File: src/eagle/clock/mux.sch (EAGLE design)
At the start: 53 parts, among them U1 SN74HC595N, U2 SN74HC595N, U3 SN74HC595N

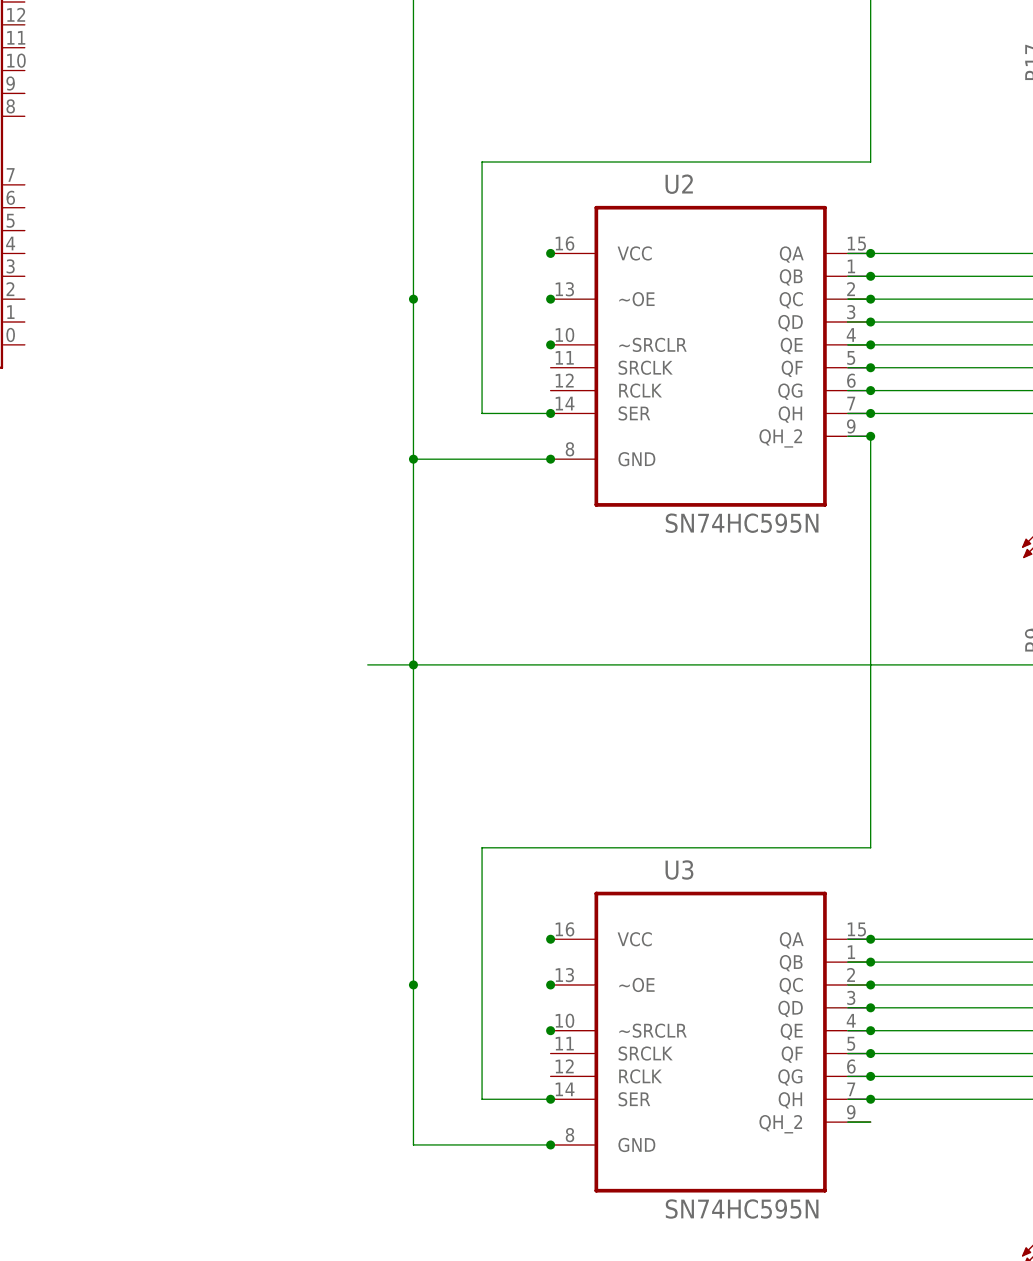
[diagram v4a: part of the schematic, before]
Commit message: cleaner connections between AR11=>SRSER
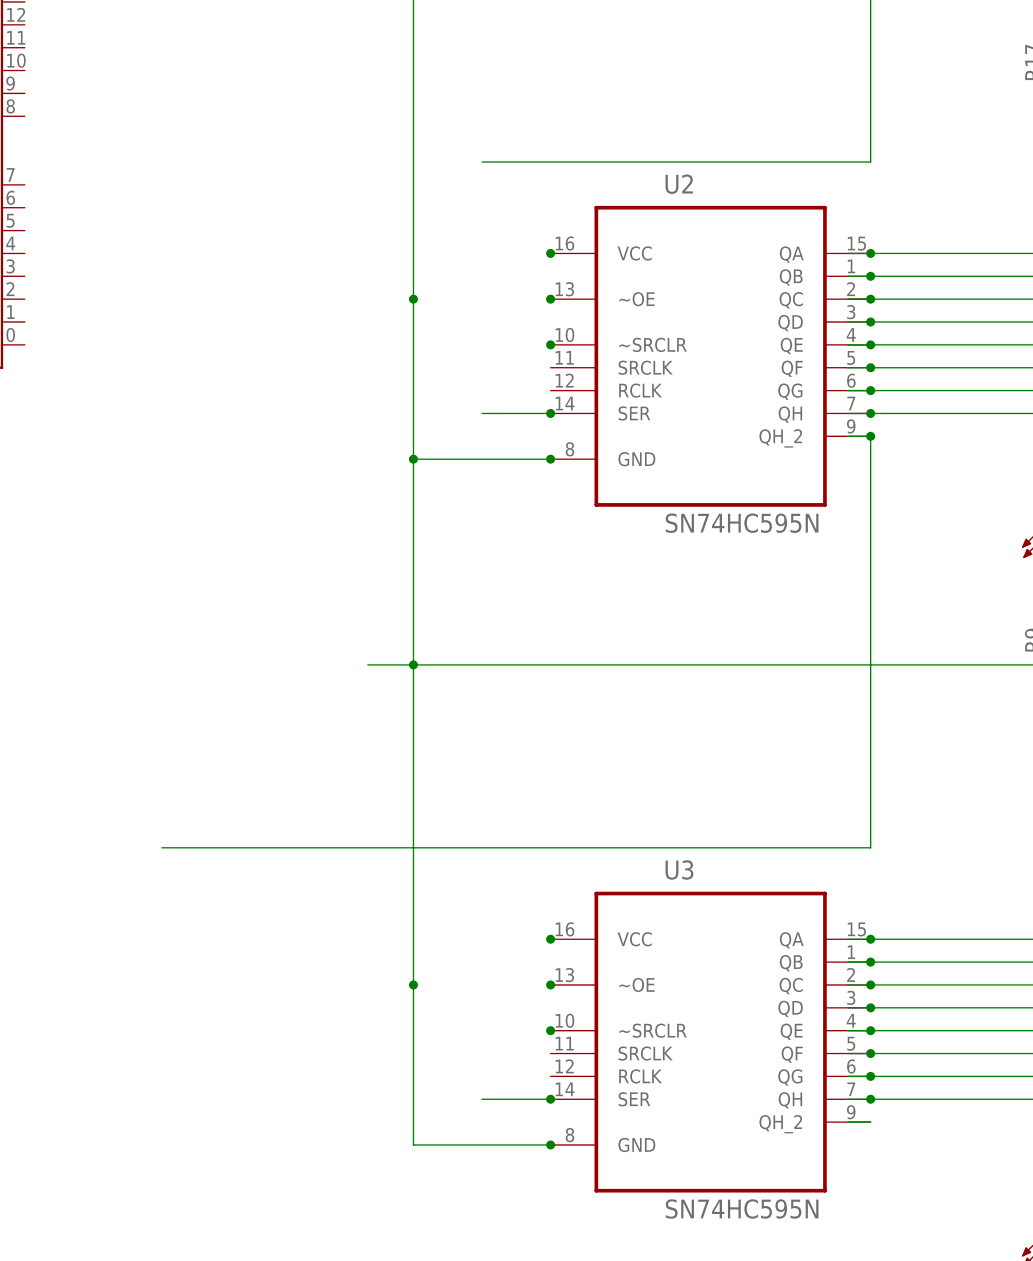
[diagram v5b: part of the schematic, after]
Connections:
- new net N$66: U2.SER
- new net N$67: U3.SER
- net N$25: no longer U2.SER
- net N$28: no longer U3.SER
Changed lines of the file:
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@@
 <wire x1="-7.62" y1="60.96" x2="-7.62" y2="50.8" width="0.1524" layer="93"/>
 <wire x1="-7.62" y1="50.8" x2="-7.62" y2="-2.54" width="0.1524" layer="93"/>
-<wire x1="-7.62" y1="-2.54" x2="20.32" y2="-2.54" width="0.1524" layer="93"/>
+<wire x1="-7.62" y1="-2.54" x2="2.54" y2="-2.54" width="0.1524" layer="93"/>
+<wire x1="7.62" y1="-2.54" x2="20.32" y2="-2.54" width="0.1524" layer="93"/>
 <wire x1="0" y1="-48.26" x2="-116.84" y2="-48.26" width="0.1524" layer="93"/>
 <wire x1="-116.84" y1="-48.26" x2="-116.84" y2="10.16" width="0.1524" layer="93"/>
@@
 <wire x1="-116.84" y1="60.96" x2="-7.62" y2="60.96" width="0.1524" layer="93"/>
 <wire x1="20.32" y1="55.88" x2="5.08" y2="55.88" width="0.1524" layer="93"/>
-<wire x1="5.08" y1="55.88" x2="5.08" y2="38.1" width="0.1524" layer="93"/>
+<wire x1="5.08" y1="55.88" x2="5.08" y2="53.34" width="0.1524" layer="93"/>
+<wire x1="5.08" y1="48.26" x2="5.08" y2="45.72" width="0.1524" layer="93"/>
+<wire x1="5.08" y1="40.64" x2="5.08" y2="38.1" width="0.1524" layer="93"/>
 <wire x1="20.32" y1="-7.62" x2="5.08" y2="-7.62" width="0.1524" layer="93"/>
 <wire x1="20.32" y1="-83.82" x2="5.08" y2="-83.82" width="0.1524" layer="93"/>
 <wire x1="20.32" y1="50.8" x2="-7.62" y2="50.8" width="0.1524" layer="93"/>
-<wire x1="20.32" y1="-12.7" x2="-7.62" y2="-12.7" width="0.1524" layer="93"/>
-<wire x1="20.32" y1="-88.9" x2="-7.62" y2="-88.9" width="0.1524" layer="93"/>
-<wire x1="-7.62" y1="-78.74" x2="20.32" y2="-78.74" width="0.1524" layer="93"/>
+<wire x1="20.32" y1="-12.7" x2="7.62" y2="-12.7" width="0.1524" layer="93"/>
+<wire x1="2.54" y1="-12.7" x2="-7.62" y2="-12.7" width="0.1524" layer="93"/>
+<wire x1="20.32" y1="-88.9" x2="7.62" y2="-88.9" width="0.1524" layer="93"/>
+<wire x1="2.54" y1="-88.9" x2="-7.62" y2="-88.9" width="0.1524" layer="93"/>
+<wire x1="-7.62" y1="-78.74" x2="2.54" y2="-78.74" width="0.1524" layer="93"/>
+<wire x1="7.62" y1="-78.74" x2="20.32" y2="-78.74" width="0.1524" layer="93"/>
+<wire x1="-38.1" y1="20.32" x2="-22.86" y2="20.32" width="0.1524" layer="93"/>
+<wire x1="-22.86" y1="20.32" x2="-22.86" y2="43.18" width="0.1524" layer="93"/>
+<wire x1="-22.86" y1="43.18" x2="-10.16" y2="43.18" width="0.1524" layer="93"/>
+<wire x1="-5.08" y1="43.18" x2="20.32" y2="43.18" width="0.1524" layer="93"/>
+<wire x1="-10.16" y1="43.18" x2="-5.08" y2="43.18" width="0.1524" layer="93" curve="-180"/>
+<wire x1="5.08" y1="53.34" x2="5.08" y2="48.26" width="0.1524" layer="93" curve="-180"/>
+<wire x1="5.08" y1="45.72" x2="5.08" y2="40.64" width="0.1524" layer="93" curve="-180"/>
+<wire x1="2.54" y1="-2.54" x2="7.62" y2="-2.54" width="0.1524" layer="93" curve="-180"/>
+<wire x1="2.54" y1="-12.7" x2="7.62" y2="-12.7" width="0.1524" layer="93" curve="-180"/>
+<wire x1="2.54" y1="-78.74" x2="7.62" y2="-78.74" width="0.1524" layer="93" curve="-180"/>
+<wire x1="12.7" y1="7.62" x2="-22.86" y2="7.62" width="0.1524" layer="93"/>
+<wire x1="-22.86" y1="7.62" x2="-22.86" y2="-20.32" width="0.1524" layer="93"/>
+<wire x1="-22.86" y1="-20.32" x2="-10.16" y2="-20.32" width="0.1524" layer="93"/>
+<wire x1="-5.08" y1="-20.32" x2="2.54" y2="-20.32" width="0.1524" layer="93"/>
+<wire x1="7.62" y1="-20.32" x2="12.7" y2="-20.32" width="0.1524" layer="93"/>
+<wire x1="-10.16" y1="-20.32" x2="-5.08" y2="-20.32" width="0.1524" layer="93" curve="-180"/>
+<wire x1="2.54" y1="-20.32" x2="7.62" y2="-20.32" width="0.1524" layer="93" curve="-180"/>
+<wire x1="-22.86" y1="-68.58" x2="-22.86" y2="-96.52" width="0.1524" layer="93"/>
+<wire x1="-22.86" y1="-96.52" x2="2.54" y2="-96.52" width="0.1524" layer="93"/>
+<wire x1="7.62" y1="-96.52" x2="12.7" y2="-96.52" width="0.1524" layer="93"/>
+<wire x1="2.54" y1="-96.52" x2="7.62" y2="-96.52" width="0.1524" layer="93" curve="-180"/>
+<wire x1="2.54" y1="-88.9" x2="7.62" y2="-88.9" width="0.1524" layer="93" curve="-180"/>
 </plain>
 <instances>
@@
 <wire x1="55.88" y1="40.64" x2="55.88" y2="7.62" width="0.1524" layer="91"/>
 <wire x1="55.88" y1="7.62" x2="12.7" y2="7.62" width="0.1524" layer="91"/>
-<wire x1="12.7" y1="7.62" x2="12.7" y2="-20.32" width="0.1524" layer="91"/>
-<pinref part="U2" gate="A" pin="SER"/>
-<wire x1="12.7" y1="-20.32" x2="20.32" y2="-20.32" width="0.1524" layer="91"/>
 <pinref part="U1" gate="A" pin="QH_2"/>
 <junction x="55.88" y="40.64"/>
-<junction x="20.32" y="-20.32"/>
 </segment>
 </net>
@@
 <wire x1="55.88" y1="-22.86" x2="53.34" y2="-22.86" width="0.1524" layer="91"/>
 <wire x1="55.88" y1="-22.86" x2="55.88" y2="-68.58" width="0.1524" layer="91"/>
-<wire x1="55.88" y1="-68.58" x2="12.7" y2="-68.58" width="0.1524" layer="91"/>
-<wire x1="12.7" y1="-68.58" x2="12.7" y2="-96.52" width="0.1524" layer="91"/>
+<wire x1="55.88" y1="-68.58" x2="-22.86" y2="-68.58" width="0.1524" layer="91"/>
+<junction x="55.88" y="-22.86"/>
+</segment>
+</net>
+<net name="N$45" class="0">
+<segment>
+<wire x1="55.88" y1="-99.06" x2="53.34" y2="-99.06" width="0.1524" layer="91"/>
+<pinref part="U3" gate="A" pin="QH_2"/>
+</segment>
+</net>
+<net name="N$47" class="0">
+<segment>
+<pinref part="U3" gate="A" pin="VCC"/>
+<junction x="20.32" y="-78.74"/>
+</segment>
+</net>
+<net name="N$48" class="0">
+<segment>
+<pinref part="U1" gate="A" pin="VCC"/>
+<junction x="20.32" y="60.96"/>
+</segment>
+</net>
+<net name="N$46" class="0">
+<segment>
+<pinref part="U2" gate="A" pin="VCC"/>
+<junction x="20.32" y="-2.54"/>
+</segment>
+</net>
+<net name="N$49" class="0">
+<segment>
+<pinref part="PCB1" gate="G$1" pin="5V"/>
+<junction x="-81.28" y="15.24"/>
+</segment>
+</net>
+<net name="N$50" class="0">
+<segment>
+<pinref part="C1" gate="G$1" pin="1"/>
+<junction x="-27.94" y="60.96"/>
+</segment>
+</net>
+<net name="N$51" class="0">
+<segment>
+<pinref part="C1" gate="G$1" pin="2"/>
+<junction x="-20.32" y="60.96"/>
+</segment>
+</net>
+<net name="N$59" class="0">
+<segment>
+<pinref part="C1" gate="G$1" pin="3"/>
+<junction x="-22.86" y="60.96"/>
+</segment>
+</net>
+<net name="N$60" class="0">
+<segment>
+<pinref part="U1" gate="A" pin="~OE"/>
+<junction x="20.32" y="55.88"/>
+</segment>
+</net>
+<net name="N$61" class="0">
+<segment>
+<pinref part="U2" gate="A" pin="~OE"/>
+<junction x="20.32" y="-7.62"/>
+</segment>
+</net>
+<net name="N$62" class="0">
+<segment>
+<pinref part="U3" gate="A" pin="~OE"/>
+<junction x="20.32" y="-83.82"/>
+</segment>
+</net>
+<net name="N$63" class="0">
+<segment>
+<pinref part="U3" gate="A" pin="~SRCLR"/>
+<junction x="20.32" y="-88.9"/>
+</segment>
+</net>
+<net name="N$64" class="0">
+<segment>
+<pinref part="U2" gate="A" pin="~SRCLR"/>
+<junction x="20.32" y="-12.7"/>
+</segment>
+</net>
+<net name="N$65" class="0">
+<segment>
+<pinref part="U1" gate="A" pin="~SRCLR"/>
+<junction x="20.32" y="50.8"/>
+</segment>
+</net>
+<net name="N$66" class="0">
+<segment>
+<pinref part="U2" gate="A" pin="SER"/>
+<wire x1="12.7" y1="-20.32" x2="20.32" y2="-20.32" width="0.1524" layer="91"/>
+<junction x="20.32" y="-20.32"/>
+</segment>
+</net>
+<net name="N$67" class="0">
+<segment>
 <pinref part="U3" gate="A" pin="SER"/>
 <wire x1="12.7" y1="-96.52" x2="20.32" y2="-96.52" width="0.1524" layer="91"/>
-<junction x="55.88" y="-22.86"/>
 <junction x="20.32" y="-96.52"/>
 </segment>
 </net>
-<net name="N$45" class="0">
-<segment>
-<wire x1="55.88" y1="-99.06" x2="53.34" y2="-99.06" width="0.1524" layer="91"/>
-<pinref part="U3" gate="A" pin="QH_2"/>
-</segment>
-</net>
-<net name="N$47" class="0">
-<segment>
-<pinref part="U3" gate="A" pin="VCC"/>
-<junction x="20.32" y="-78.74"/>
-</segment>
-</net>
-<net name="N$48" class="0">
-<segment>
-<pinref part="U1" gate="A" pin="VCC"/>
-<junction x="20.32" y="60.96"/>
-</segment>
-</net>
-<net name="N$46" class="0">
-<segment>
-<pinref part="U2" gate="A" pin="VCC"/>
-<junction x="20.32" y="-2.54"/>
-</segment>
-</net>
-<net name="N$49" class="0">
-<segment>
-<pinref part="PCB1" gate="G$1" pin="5V"/>
-<junction x="-81.28" y="15.24"/>
-</segment>
-</net>
-<net name="N$50" class="0">
-<segment>
-<pinref part="C1" gate="G$1" pin="1"/>
-<junction x="-27.94" y="60.96"/>
-</segment>
-</net>
-<net name="N$51" class="0">
-<segment>
-<pinref part="C1" gate="G$1" pin="2"/>
-<junction x="-20.32" y="60.96"/>
-</segment>
-</net>
-<net name="N$59" class="0">
-<segment>
-<pinref part="C1" gate="G$1" pin="3"/>
-<junction x="-22.86" y="60.96"/>
-</segment>
-</net>
-<net name="N$60" class="0">
-<segment>
-<pinref part="U1" gate="A" pin="~OE"/>
-<junction x="20.32" y="55.88"/>
-</segment>
-</net>
-<net name="N$61" class="0">
-<segment>
-<pinref part="U2" gate="A" pin="~OE"/>
-<junction x="20.32" y="-7.62"/>
-</segment>
-</net>
-<net name="N$62" class="0">
-<segment>
-<pinref part="U3" gate="A" pin="~OE"/>
-<junction x="20.32" y="-83.82"/>
-</segment>
-</net>
-<net name="N$63" class="0">
-<segment>
-<pinref part="U3" gate="A" pin="~SRCLR"/>
-<junction x="20.32" y="-88.9"/>
-</segment>
-</net>
-<net name="N$64" class="0">
-<segment>
-<pinref part="U2" gate="A" pin="~SRCLR"/>
-<junction x="20.32" y="-12.7"/>
-</segment>
-</net>
-<net name="N$65" class="0">
-<segment>
-<pinref part="U1" gate="A" pin="~SRCLR"/>
-<junction x="20.32" y="50.8"/>
-</segment>
-</net>
